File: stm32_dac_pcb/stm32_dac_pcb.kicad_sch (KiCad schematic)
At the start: 11 parts, among them U203 AP1117-33

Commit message: Bump to KiCAD v8
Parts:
- renumbered C205 to C101, C205 to C102, C205 to C103, C205 to C104, U203 to U101, U203 to U102

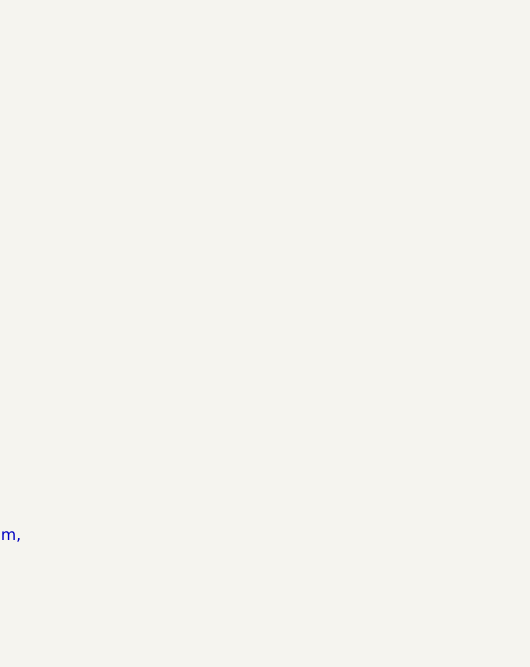
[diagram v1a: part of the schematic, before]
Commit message: Add LED, layout
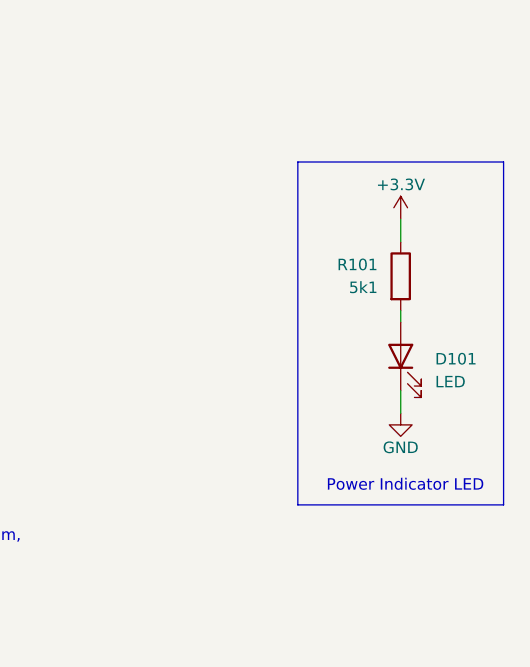
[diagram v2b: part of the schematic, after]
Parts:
- added D101: LED, LED_SMD:LED_0603_1608Metric_Pad1.05x0.95mm_HandSolder, symbol Device:LED
- added R101: 5k1, Resistor_SMD:R_0603_1608Metric_Pad0.98x0.95mm_HandSolder, symbol Device:R
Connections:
- net +3.3V: now also R101.1
- net GND: now also D101.1 (K)
- new net: D101.2 (A), R101.2
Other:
- note added: "Power Indicator LED"

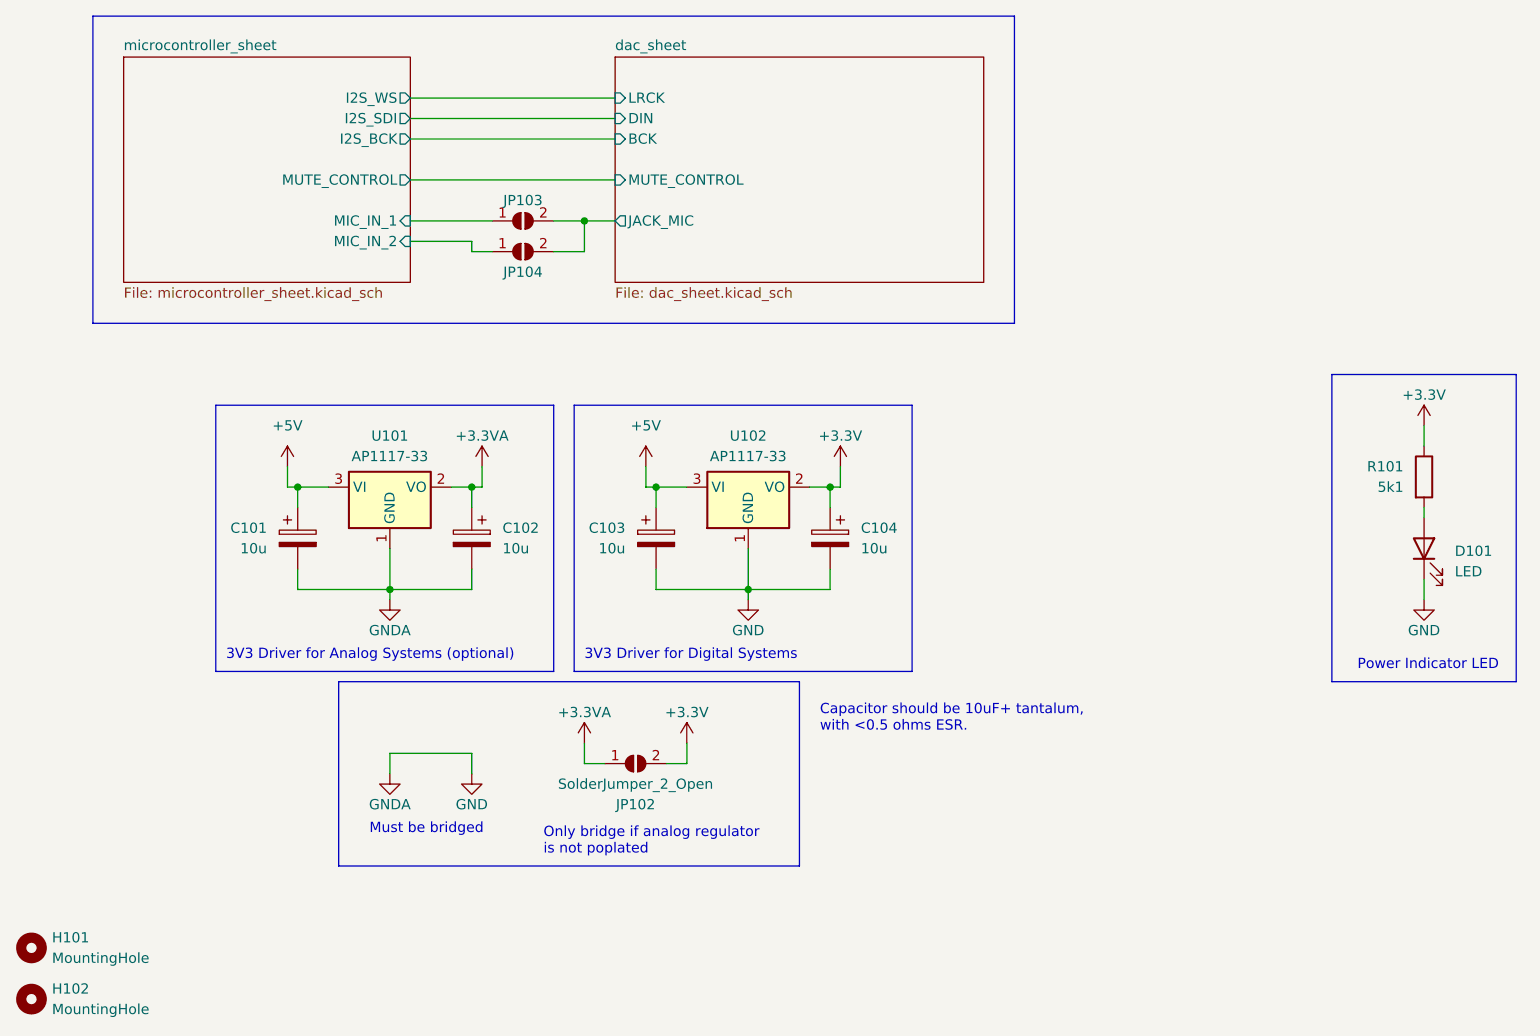
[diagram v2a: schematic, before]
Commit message: Finish layout with crystal
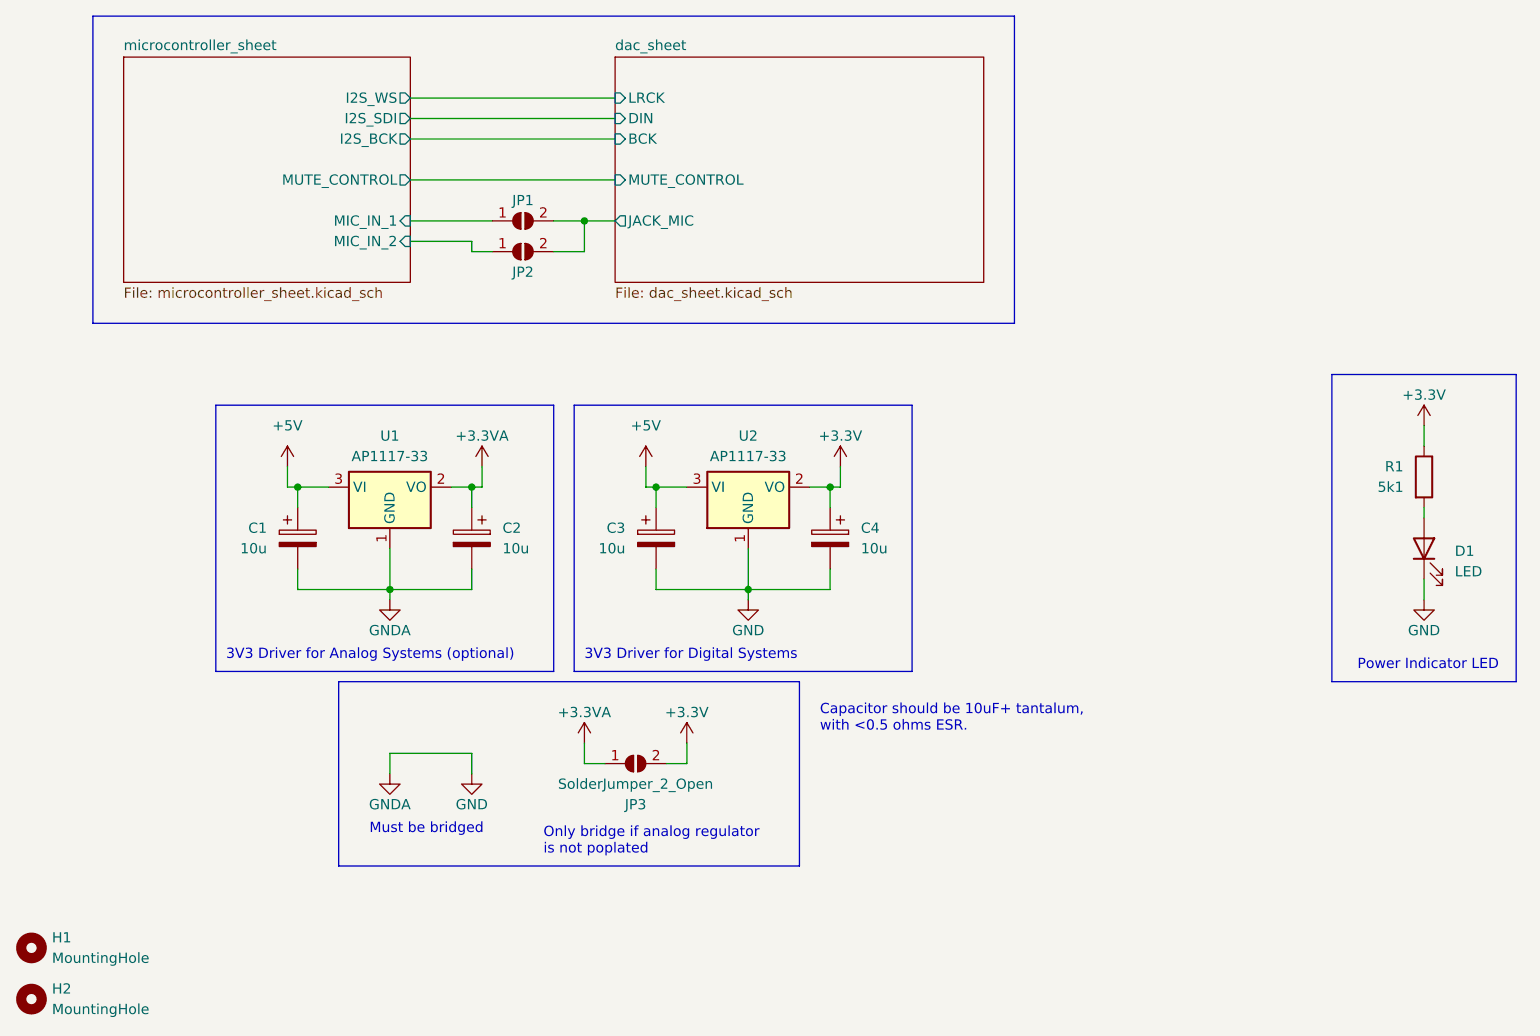
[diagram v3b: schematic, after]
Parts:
- renumbered C101 to C1, C102 to C2, C103 to C3, C104 to C4, D101 to D1, H101 to H1, H102 to H2, JP103 to JP1, JP104 to JP2, JP102 to JP3, R101 to R1, U101 to U1, U102 to U2
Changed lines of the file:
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@@
 		(on_board yes)
 		(dnp no)
-		(property "Reference" "C101"
+		(property "Reference" "C1"
 			(at 48.26 130.81 0)
 			(effects
@@
 			(project "stm32_dac_pcb"
 				(path "/c2a919d7-4260-41a9-9bc5-9737c1b4d769"
-					(reference "C101")
+					(reference "C1")
 					(unit 1)
 				)
@@
 		(on_board yes)
 		(dnp no)
-		(property "Reference" "#PWR0106"
+		(property "Reference" "#PWR010"
 			(at 119.38 127 0)
 			(effects
@@
 			(project "stm32_dac_pcb"
 				(path "/c2a919d7-4260-41a9-9bc5-9737c1b4d769"
-					(reference "#PWR0106")
+					(reference "#PWR010")
 					(unit 1)
 				)
@@
 		(on_board yes)
 		(dnp no)
-		(property "Reference" "#PWR0105"
+		(property "Reference" "#PWR09"
 			(at 107.95 146.05 0)
 			(effects
@@
 			(project "stm32_dac_pcb"
 				(path "/c2a919d7-4260-41a9-9bc5-9737c1b4d769"
-					(reference "#PWR0105")
+					(reference "#PWR09")
 					(unit 1)
 				)
@@
 		(dnp no)
 		(fields_autoplaced yes)
-		(property "Reference" "H102"
+		(property "Reference" "H2"
 			(at 21.59 187.96 0)
 			(effects
@@
 			(project "stm32_dac_pcb"
 				(path "/c2a919d7-4260-41a9-9bc5-9737c1b4d769"
-					(reference "H102")
+					(reference "H2")
 					(unit 1)
 				)
@@
 		(dnp no)
 		(fields_autoplaced yes)
-		(property "Reference" "U102"
+		(property "Reference" "U2"
 			(at 107.95 119.38 0)
 			(effects
@@
 			(project "stm32_dac_pcb"
 				(path "/c2a919d7-4260-41a9-9bc5-9737c1b4d769"
-					(reference "U102")
+					(reference "U2")
 					(unit 1)
 				)
@@
 		(on_board yes)
 		(dnp no)
-		(property "Reference" "#PWR0102"
+		(property "Reference" "#PWR02"
 			(at 63.5 146.05 0)
 			(effects
@@
 			(project "stm32_dac_pcb"
 				(path "/c2a919d7-4260-41a9-9bc5-9737c1b4d769"
-					(reference "#PWR0102")
+					(reference "#PWR02")
 					(unit 1)
 				)
@@
 		(on_board yes)
 		(dnp no)
-		(property "Reference" "#PWR0103"
+		(property "Reference" "#PWR05"
 			(at 74.93 127 0)
 			(effects
@@
 			(project "stm32_dac_pcb"
 				(path "/c2a919d7-4260-41a9-9bc5-9737c1b4d769"
-					(reference "#PWR0103")
+					(reference "#PWR05")
 					(unit 1)
 				)
@@
 		(on_board yes)
 		(dnp no)
-		(property "Reference" "R101"
+		(property "Reference" "R1"
 			(at 189.23 123.19 0)
 			(effects
@@
 			(project "stm32_dac_pcb"
 				(path "/c2a919d7-4260-41a9-9bc5-9737c1b4d769"
-					(reference "R101")
+					(reference "R1")
 					(unit 1)
 				)
@@
 		(dnp no)
 		(fields_autoplaced yes)
-		(property "Reference" "#PWR0101"
+		(property "Reference" "#PWR01"
 			(at 50.8 127 0)
 			(effects
@@
 			(project "stm32_dac_pcb"
 				(path "/c2a919d7-4260-41a9-9bc5-9737c1b4d769"
-					(reference "#PWR0101")
+					(reference "#PWR01")
 					(unit 1)
 				)
@@
 		(dnp no)
 		(fields_autoplaced yes)
-		(property "Reference" "D101"
+		(property "Reference" "D1"
 			(at 195.58 133.6674 90)
 			(effects
@@
 			(project ""
 				(path "/c2a919d7-4260-41a9-9bc5-9737c1b4d769"
-					(reference "D101")
+					(reference "D1")
 					(unit 1)
 				)
@@
 		(on_board yes)
 		(dnp no)
-		(property "Reference" "C103"
+		(property "Reference" "C3"
 			(at 92.71 130.81 0)
 			(effects
@@
 			(project "stm32_dac_pcb"
 				(path "/c2a919d7-4260-41a9-9bc5-9737c1b4d769"
-					(reference "C103")
+					(reference "C3")
 					(unit 1)
 				)
@@
 		(on_board yes)
 		(dnp no)
-		(property "Reference" "#PWR0107"
+		(property "Reference" "#PWR03"
 			(at 63.5 167.64 0)
 			(effects
@@
 			(project "stm32_dac_pcb"
 				(path "/c2a919d7-4260-41a9-9bc5-9737c1b4d769"
-					(reference "#PWR0107")
+					(reference "#PWR03")
 					(unit 1)
 				)
@@
 		(on_board yes)
 		(dnp no)
-		(property "Reference" "#PWR0108"
+		(property "Reference" "#PWR04"
 			(at 73.66 167.64 0)
 			(effects
@@
 			(project "stm32_dac_pcb"
 				(path "/c2a919d7-4260-41a9-9bc5-9737c1b4d769"
-					(reference "#PWR0108")
+					(reference "#PWR04")
 					(unit 1)
 				)
@@
 		(on_board yes)
 		(dnp no)
-		(property "Reference" "C102"
+		(property "Reference" "C2"
 			(at 77.47 130.81 0)
 			(effects
@@
 			(project "stm32_dac_pcb"
 				(path "/c2a919d7-4260-41a9-9bc5-9737c1b4d769"
-					(reference "C102")
+					(reference "C2")
 					(unit 1)
 				)
@@
 		(on_board yes)
 		(dnp no)
-		(property "Reference" "#PWR0111"
+		(property "Reference" "#PWR012"
 			(at 191.77 146.05 0)
 			(effects
@@
 			(project "stm32_dac_pcb"
 				(path "/c2a919d7-4260-41a9-9bc5-9737c1b4d769"
-					(reference "#PWR0111")
+					(reference "#PWR012")
 					(unit 1)
 				)
@@
 		(on_board yes)
 		(dnp no)
-		(property "Reference" "JP104"
+		(property "Reference" "JP2"
 			(at 80.01 99.06 0)
 			(effects
@@
 			(project "stm32_dac_pcb"
 				(path "/c2a919d7-4260-41a9-9bc5-9737c1b4d769"
-					(reference "JP104")
+					(reference "JP2")
 					(unit 1)
 				)
@@
 		(on_board yes)
 		(dnp no)
-		(property "Reference" "#PWR0110"
+		(property "Reference" "#PWR06"
 			(at 87.63 161.29 0)
 			(effects
@@
 			(project "stm32_dac_pcb"
 				(path "/c2a919d7-4260-41a9-9bc5-9737c1b4d769"
-					(reference "#PWR0110")
+					(reference "#PWR06")
 					(unit 1)
 				)
@@
 		(on_board yes)
 		(dnp no)
-		(property "Reference" "#PWR0112"
+		(property "Reference" "#PWR011"
 			(at 191.77 121.92 0)
 			(effects
@@
 			(project "stm32_dac_pcb"
 				(path "/c2a919d7-4260-41a9-9bc5-9737c1b4d769"
-					(reference "#PWR0112")
+					(reference "#PWR011")
 					(unit 1)
 				)
@@
 		(on_board yes)
 		(dnp no)
-		(property "Reference" "JP102"
+		(property "Reference" "JP3"
 			(at 93.98 165.1 0)
 			(effects
@@
 			(project "stm32_dac_pcb"
 				(path "/c2a919d7-4260-41a9-9bc5-9737c1b4d769"
-					(reference "JP102")
+					(reference "JP3")
 					(unit 1)
 				)
@@
 		(on_board yes)
 		(dnp no)
-		(property "Reference" "#PWR0109"
+		(property "Reference" "#PWR08"
 			(at 100.33 161.29 0)
 			(effects
@@
 			(project "stm32_dac_pcb"
 				(path "/c2a919d7-4260-41a9-9bc5-9737c1b4d769"
-					(reference "#PWR0109")
+					(reference "#PWR08")
 					(unit 1)
 				)
@@
 		(dnp no)
 		(fields_autoplaced yes)
-		(property "Reference" "U101"
+		(property "Reference" "U1"
 			(at 63.5 119.38 0)
 			(effects
@@
 			(project "stm32_dac_pcb"
 				(path "/c2a919d7-4260-41a9-9bc5-9737c1b4d769"
-					(reference "U101")
+					(reference "U1")
 					(unit 1)
 				)
@@
 		(on_board yes)
 		(dnp no)
-		(property "Reference" "C104"
+		(property "Reference" "C4"
 			(at 121.92 130.81 0)
 			(effects
@@
 			(project "stm32_dac_pcb"
 				(path "/c2a919d7-4260-41a9-9bc5-9737c1b4d769"
-					(reference "C104")
+					(reference "C4")
 					(unit 1)
 				)
@@
 		(dnp no)
 		(fields_autoplaced yes)
-		(property "Reference" "H101"
+		(property "Reference" "H1"
 			(at 21.59 181.61 0)
 			(effects
@@
 			(project "stm32_dac_pcb"
 				(path "/c2a919d7-4260-41a9-9bc5-9737c1b4d769"
-					(reference "H101")
+					(reference "H1")
 					(unit 1)
 				)
@@
 		(dnp no)
 		(fields_autoplaced yes)
-		(property "Reference" "#PWR0104"
+		(property "Reference" "#PWR07"
 			(at 95.25 127 0)
 			(effects
@@
 			(project "stm32_dac_pcb"
 				(path "/c2a919d7-4260-41a9-9bc5-9737c1b4d769"
-					(reference "#PWR0104")
+					(reference "#PWR07")
 					(unit 1)
 				)
@@
 		(on_board yes)
 		(dnp no)
-		(property "Reference" "JP103"
+		(property "Reference" "JP1"
 			(at 80.01 90.17 0)
 			(effects
@@
 			(project "stm32_dac_pcb"
 				(path "/c2a919d7-4260-41a9-9bc5-9737c1b4d769"
-					(reference "JP103")
-					(unit 1)
-				)
+					(reference "JP1")
+					(unit 1)
+				)
